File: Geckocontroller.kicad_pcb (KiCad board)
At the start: 2 copper layers, 108.5 x 94.2 mm, 90 parts, among them J101 AC Input, J19 I²C (BME280), J21 RGB LED, J31 DS18B20 I, J32 DS18B20 II, J40 Fan Connector, J51 USB_C_Receptacle_USB2.0, J61 Load Cell Connector, J70 SPI / Addon Connector, J81 Dimmer, J91 Pump, J92 HeatBed, J93 HeatLamp, K81 AQG12212, K91 AQG12112, K92 AQG12112, K93 AQG12112, Q21 AO3400A, Q222 AO3400A, Q23 AO3400A, Q51 S8050, Q52 S8050, Q61 S8550, Q81 AO3400A, Q91 AO3400A, Q92 AO3400A, Q93 AO3400A, SW1 SW_Push, U1 ESP32-WROOM-32, U101 ACT4088, U2 CP2102, U61 HX711, U81 6N138

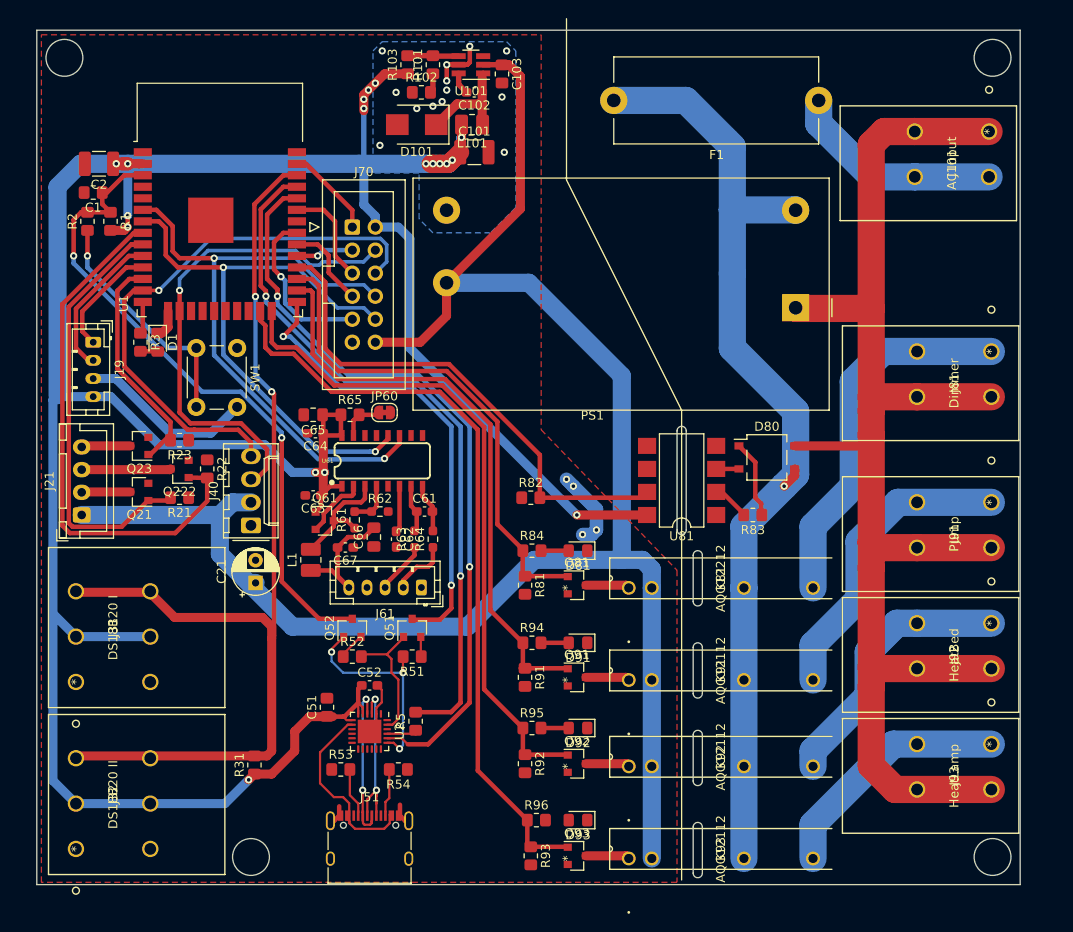
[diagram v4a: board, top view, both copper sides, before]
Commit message: PCB: Silkscreen Inscriptions
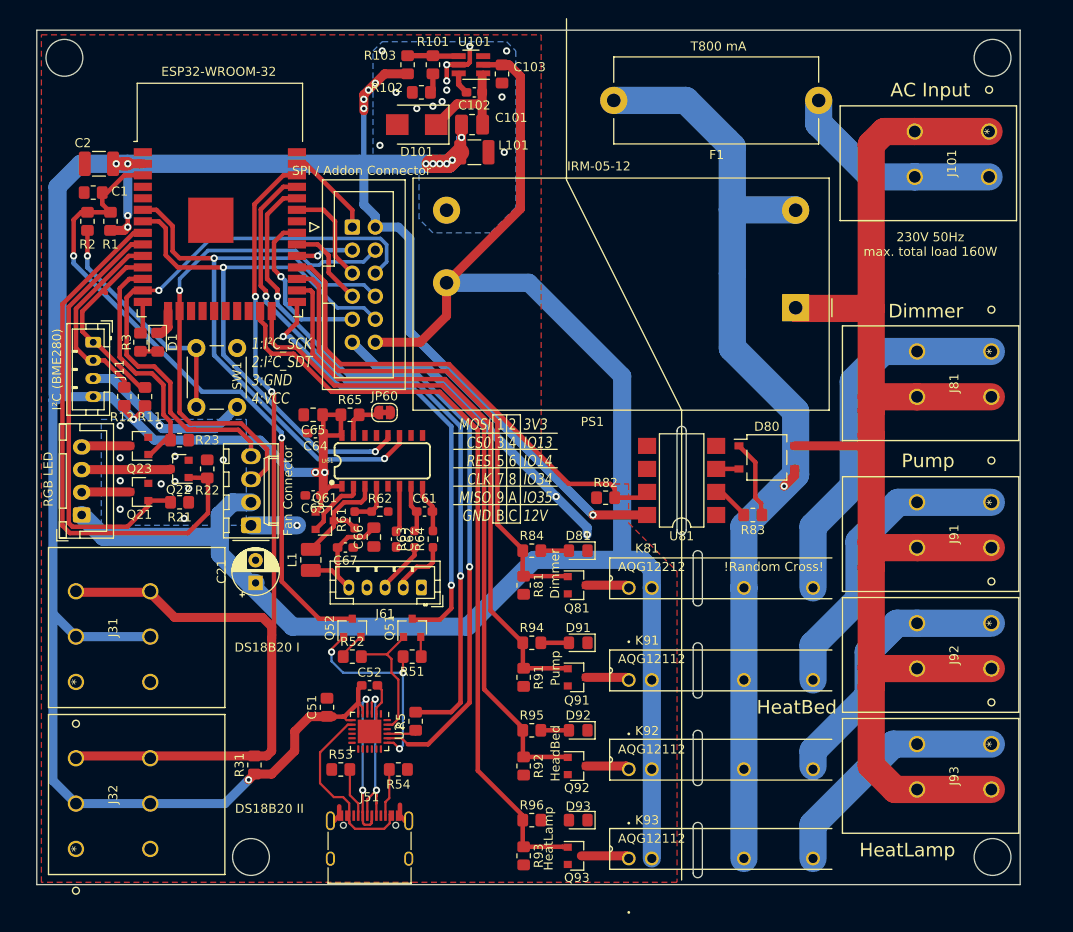
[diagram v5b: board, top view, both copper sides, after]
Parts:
- added R11: 4k7, Resistor_SMD:R_0805_2012Metric_Pad1.20x1.40mm_HandSolder, F.Cu at (29.2, 53.6)
- added R12: 4k7, Resistor_SMD:R_0805_2012Metric_Pad1.20x1.40mm_HandSolder, F.Cu at (26.9, 53.6)
- R101: value 18k+1% -> 18k±1%
- R102: value 220R+1% -> 226R±1%
- R103: value 47k+1% -> 47k±1%
- moved R82 8.26 mm to (80.0, 64.8)
- moved R93 0.79 mm to (71.0, 104.3)
- moved R21 0.51 mm to (33.0, 65.3)
- moved R96 0.51 mm to (71.9, 100.3)
- moved K92 0.32 mm to (92.7, 93.7)
- moved R92 0.30 mm to (71.0, 94.4)
- moved D92 0.26 mm to (77.0, 90.4)
- moved R95 0.25 mm to (71.9, 90.4)
- moved Q92 0.25 mm to (76.8, 94.4)
- moved R81 0.15 mm to (71.0, 74.4)
- moved R91 0.15 mm to (71.0, 84.6)
- renumbered J19 to J11, Q222 to Q22
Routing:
- net GND: track 48.9 -> 80.0 mm, vias 17 -> 27
- net /I2C_SCK: track 12.6 -> 20.8 mm
- net /I2C_SDI: track 16.6 -> 21.7 mm
- net +12V: track 227.3 -> 230.8 mm
- net +3V3: track 322.1 -> 325.0 mm, vias 18 -> 19
- net /ZX_in: track 56.8 -> 54.5 mm
- net /Red_out: track 58.9 -> 59.8 mm
- net FAN_PWM: track 62.7 -> 63.6 mm
- net /Blue_out: track 26.0 -> 26.8 mm
- net Net-(K93-Pad-): track 4.85 -> 5.36 mm
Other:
- board text added: "!Random Cross!"
- board text added: "1 2 3 4 5 6 7 8 9 A B C"
- board text added: "1:I²C_SCK 2:I²C_SDT 3:GND 4:VCC"
- board text added: "230V 50Hz max. total load 160W"
- board text added: "3V3 IO13 IO14 IO34 IO35 12V"
- board text added: "Dimmer"
- board text added: "HeadBed"
- board text added: "HeatLamp"
- board text added: "MOSI CS0 RES CLK MISO GND"
- board text added: "Pump"

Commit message: PCB: Silkscreen Inscriptions + Logo
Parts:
- added REF**: OSHW-Logo_5.7x6mm_Copper, Symbol:OSHW-Logo_5.7x6mm_Copper, F.Cu at (62.2, 96.0)
- PS1: value IRM-05-12 -> MeanWell IRM-05-12
- moved J11 6.03 mm to (22.6, 53.6), turned to 90 degrees
- moved JP60 0.25 mm to (55.6, 55.6)
- renumbered F1 to Fuse1
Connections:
- J11 pad 1: /I2C_SCK -> +3V3
- J11 pad 2: /I2C_SDI -> GND
- J11 pad 3: GND -> /I2C_SDI
- J11 pad 4: +3V3 -> /I2C_SCK
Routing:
- net GND: track 80.0 -> 80.9 mm
- net /I2C_SCK: track 20.8 -> 21.6 mm
- net /I2C_SDI: track 21.7 -> 22.3 mm
- net HX_DATA: track 64.5 -> 65.1 mm
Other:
- board text added: "+"
- board text added: "1"
- board text added: "1 3 5 7 9 B"
- board text added: "2"
- board text added: "2 4 6 8 A C"
- board text added: "230V 50Hz max. load 160W total"
- board text added: "3"
- board text added: "4"
- board text added: "4 3 2 1"
- board text added: "5"
- board text added: "DS 3V3 GND"
- board text added: "E+ E- A- A+ Shi"
- board text added: "Fraxinas"
- board text added: "GeckoControl"
- board text added: "L"
- board text added: "Load Cell Connector"
- board text added: "MOSI CS0 RST CLK MISO GND"
- board text added: "N"
- board text added: "Red Black White Green Yellow"
- board text added: "Reset"
- board text added: "SCK SDA GND VCC"
- board text added: "SPI/Addon Connector"
- board text added: "Yel Red Blk"
- board text added: "closed=80SPS open=10SPS"
- board text added: "v.1 2/2021"
- board text removed: "1 2 3 4 5 6 7 8 9 A B C"
- board text removed: "1:I²C_SCK 2:I²C_SDT 3:GND 4:VCC"
- board text removed: "230V 50Hz max. total load 160W"
- board text removed: "MOSI CS0 RES CLK MISO GND"

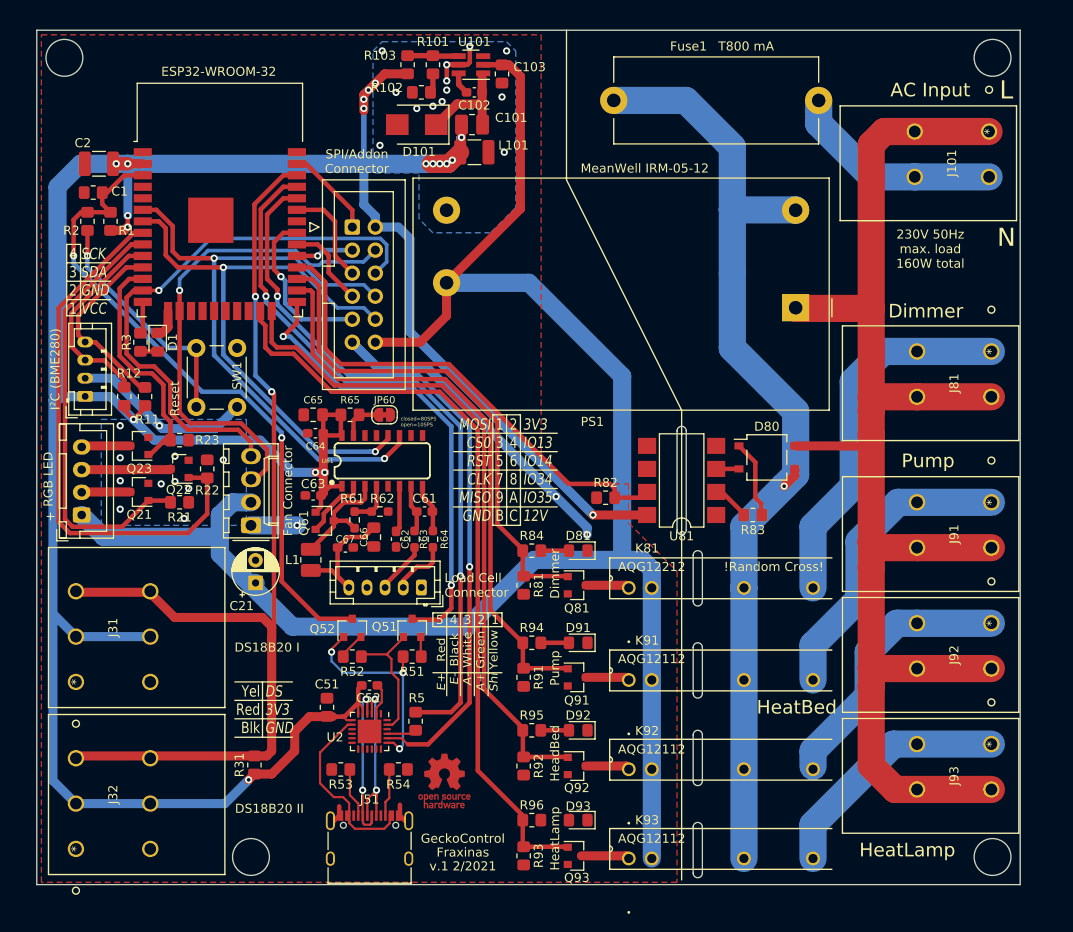
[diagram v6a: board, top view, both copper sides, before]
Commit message: PCB: More GND planes & vias, work on silkscreen inscriptions
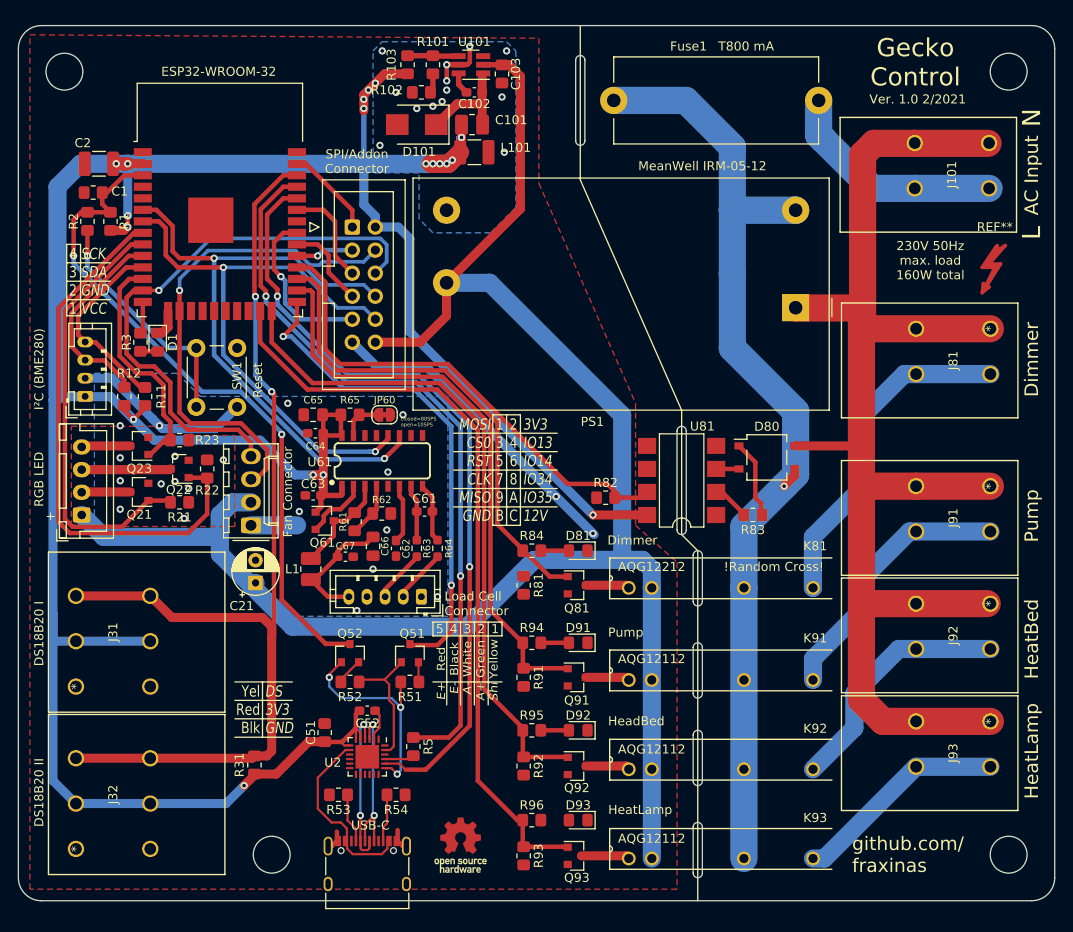
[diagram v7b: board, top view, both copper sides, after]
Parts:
- removed the REF** at (62.2, 96.0)
- added REF**: Symbol_Highvoltage_Type1_CopperTop_Small, Symbol:Symbol_Highvoltage_Type1_CopperTop_Small, F.Cu at (121.9, 40.1)
- added REF**: OSHW-Logo_5.7x6mm_Mask, footprints:OSHW-Logo_5.7x6mm_Mask, F.Cu at (64.0, 103.1)
- J51: value USB_C_Receptacle_USB2.0 -> USB-C
- R101: value 18k±1% -> 15k±1%
- R102: value 226R±1% -> 287R±1%
- R61: value R -> 47k±1%; footprint Resistor_SMD:R_0603_1608Metric_Pad0.98x0.95mm_HandSolder -> Resistor_SMD:R_0805_2012Metric_Pad1.20x1.40mm_HandSolder
- R62: value R -> 30k1±1%; footprint Resistor_SMD:R_0603_1608Metric_Pad0.98x0.95mm_HandSolder -> Resistor_SMD:R_0805_2012Metric_Pad1.20x1.40mm_HandSolder
- moved J51 2.81 mm to (53.7, 106.3)
- moved Q51 2.81 mm to (58.4, 81.9)
- moved Q52 2.81 mm to (51.8, 81.9)
- moved C51 2.81 mm to (49.0, 90.7)
- moved C52 2.81 mm to (53.7, 88.3)
- moved U2 2.81 mm to (53.7, 93.3)
- moved R5 2.81 mm to (58.8, 92.2)
- moved R51 2.81 mm to (58.4, 85.1)
- moved R52 2.81 mm to (51.8, 85.1)
- moved R53 2.81 mm to (50.5, 97.5)
- moved R54 2.81 mm to (56.9, 97.5)
- moved J81 2.51 mm to (122.4, 46.1)
- moved J93 2.51 mm to (122.4, 89.4)
- moved J92 2.16 mm to (122.4, 76.5)
- moved J91 1.78 mm to (122.4, 63.5)
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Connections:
- J81 pad 1: /L_Dimmer -> /N
- J81 pad 2: /L_Dimmer -> /N
- J81 pad 3: /N -> /L_Dimmer
- J81 pad 4: /N -> /L_Dimmer
- J91 pad 1: /L_Relay1 -> /N
- J91 pad 2: /L_Relay1 -> /N
- J91 pad 3: /N -> /L_Relay1
- J91 pad 4: /N -> /L_Relay1
- J92 pad 1: /L_Relay2 -> /N
- J92 pad 2: /L_Relay2 -> /N
- J92 pad 3: /N -> /L_Relay2
- J92 pad 4: /N -> /L_Relay2
- J93 pad 1: /L_Relay3 -> /N
- J93 pad 2: /L_Relay3 -> /N
- J93 pad 3: /N -> /L_Relay3
- J93 pad 4: /N -> /L_Relay3
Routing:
- net /N: track 153.8 -> 148.5 mm
- net /L_Relay1: track 33.8 -> 29.7 mm
- net /L_Dimmer: track 41.2 -> 37.3 mm
- net /L_Relay3: track 27.1 -> 23.8 mm
- net RXD: track 83.0 -> 85.9 mm
- net IO0: track 52.0 -> 54.9 mm
- net /TXD': track 78.5 -> 81.4 mm
- net /L_Relay2: track 30.0 -> 27.3 mm
- net +12V: track 230.8 -> 228.2 mm
- net /L: track 23.8 -> 25.9 mm
- net EN: track 73.6 -> 75.7 mm
- net /Dimmer_out: track 55.9 -> 54.2 mm
- net /AVDD: track 12.9 -> 11.3 mm
- net Net-(C62-Pad1): track 5.13 -> 6.46 mm
- net Net-(C61-Pad2): track 5.40 -> 6.62 mm
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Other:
- board size 108.5 x 94.2 mm -> 114.3 x 96.5 mm
- board text added: "Gecko Control"
- board text added: "Ver. 1.0 2/2021"
- board text added: "github.com/ fraxinas"
- board text removed: "Fraxinas"
- board text removed: "GeckoControl"
- board text removed: "v.1 2/2021"

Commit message: PCB: Decrease distance of WAGO terminals
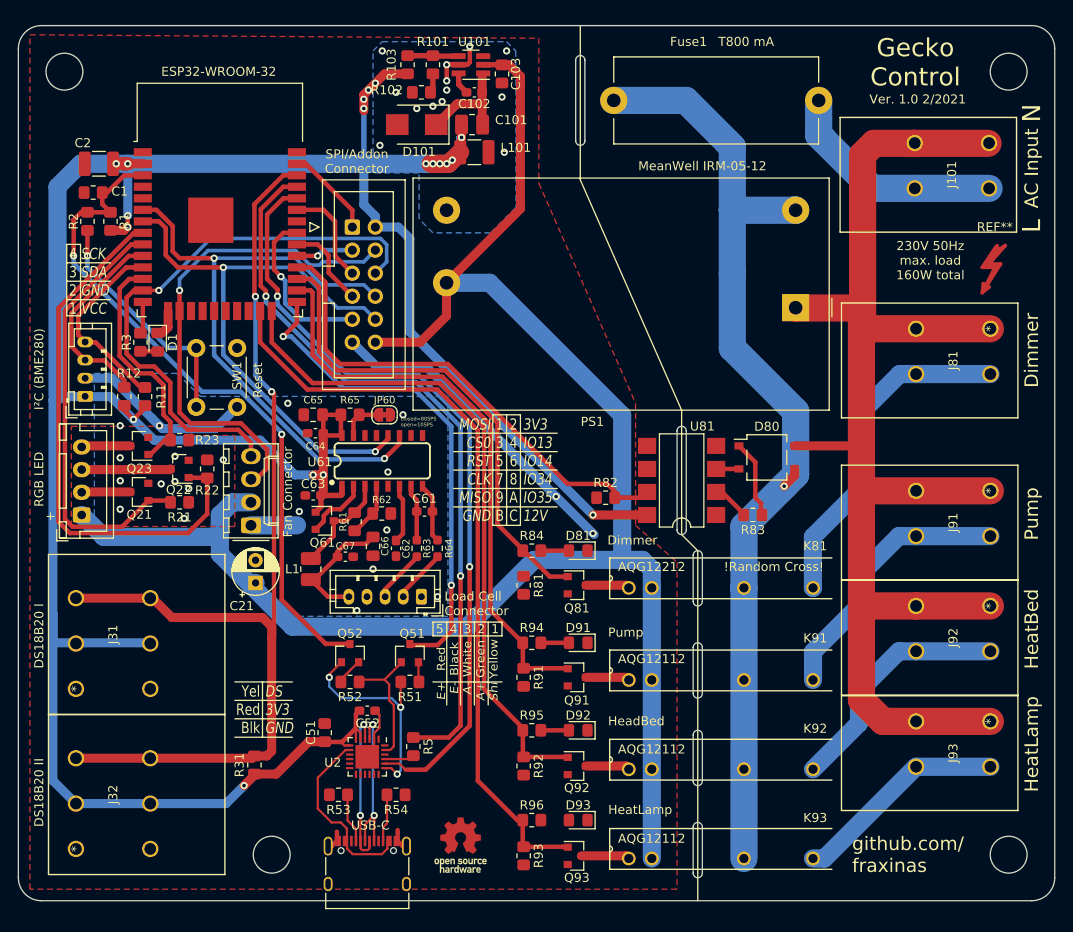
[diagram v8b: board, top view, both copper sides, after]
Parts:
- moved J91 0.51 mm to (122.4, 64.0)
- moved J31 0.25 mm to (21.6, 85.9)
- moved J92 0.25 mm to (122.4, 76.7)
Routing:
- net /N: track 148.5 -> 147.4 mm
